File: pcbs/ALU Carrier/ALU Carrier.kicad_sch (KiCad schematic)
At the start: 2 parts, among them J1001 Conn_02x20_Odd_Even, J1002 Conn_02x20_Odd_Even

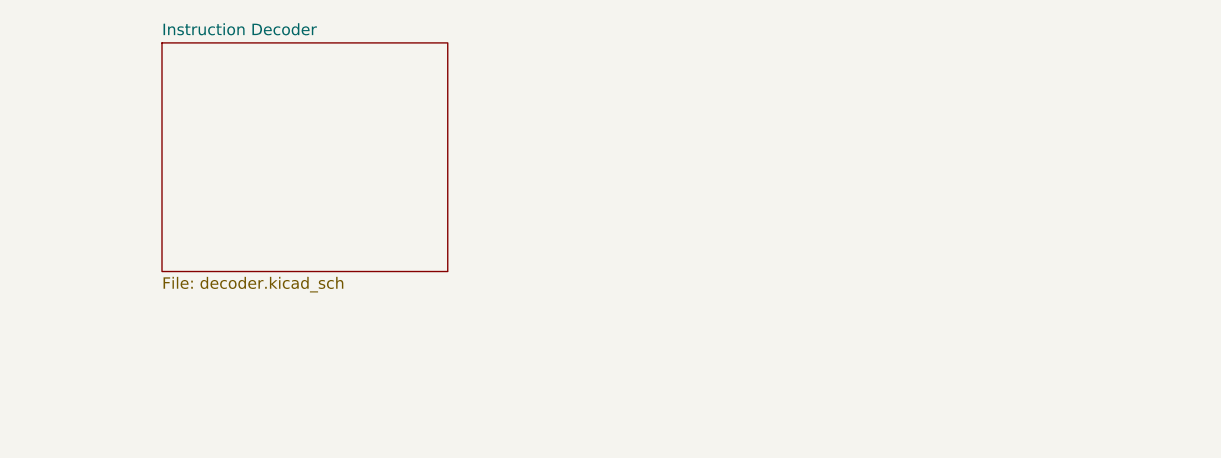
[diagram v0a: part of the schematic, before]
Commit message: Adding the adder
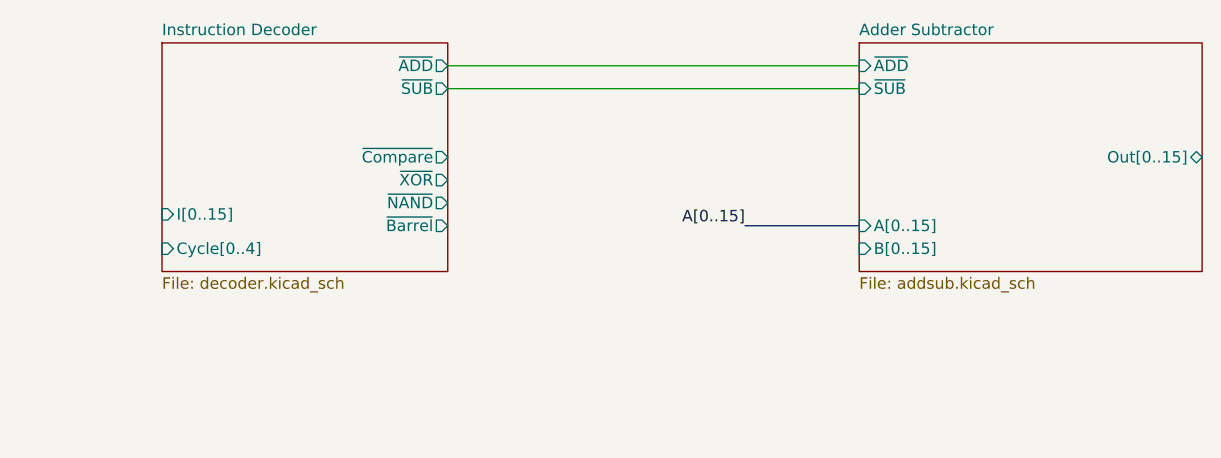
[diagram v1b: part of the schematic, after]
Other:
- added sheet Adder Subtractor (addsub.kicad_sch)
- sheet Instruction Decoder ports: added Cycle[0..4], I[0..15], ~{ADD}, ~{Barrel}, ~{Compare}, ~{NAND}, ~{SUB}, ~{XOR}; removed none
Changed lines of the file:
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@@
 	(generator "eeschema")
 	(generator_version "8.0")
-	(paper "A4")
+	(paper "A3")
 	(no_connect
 		(at 44.45 76.2)
@@
 	(wire
 		(pts
+			(xy 132.08 27.94) (xy 177.8 27.94)
+		)
+		(stroke
+			(width 0)
+			(type default)
+		)
+	)
+	(wire
+		(pts
 			(xy 44.45 128.27) (xy 46.99 128.27)
 		)
@@
 	(wire
 		(pts
+			(xy 132.08 30.48) (xy 177.8 30.48)
+		)
+		(stroke
+			(width 0)
+			(type default)
+		)
+	)
+	(wire
+		(pts
 			(xy 44.45 143.51) (xy 46.99 143.51)
 		)
@@
 		(pts
 			(xy 29.21 140.97) (xy 31.75 140.97)
+		)
+		(stroke
+			(width 0)
+			(type default)
+		)
+	)
+	(bus
+		(pts
+			(xy 165.1 45.72) (xy 177.8 45.72)
 		)
 		(stroke
@@
 	(label "I10"
 		(at 29.21 128.27 180)
+		(fields_autoplaced yes)
+		(effects
+			(font
+				(size 1.27 1.27)
+			)
+			(justify right bottom)
+		)
+	)
+	(label "A[0..15]"
+		(at 165.1 45.72 180)
 		(fields_autoplaced yes)
 		(effects
@@
 			)
 		)
+		(pin "I[0..15]" input
+			(at 100.33 44.45 180)
+			(effects
+				(font
+					(size 1.27 1.27)
+				)
+				(justify left)
+			)
+		)
+		(pin "Cycle[0..4]" input
+			(at 100.33 48.26 180)
+			(effects
+				(font
+					(size 1.27 1.27)
+				)
+				(justify left)
+			)
+		)
+		(pin "~{XOR}" output
+			(at 132.08 40.64 0)
+			(effects
+				(font
+					(size 1.27 1.27)
+				)
+				(justify right)
+			)
+		)
+		(pin "~{Compare}" output
+			(at 132.08 38.1 0)
+			(effects
+				(font
+					(size 1.27 1.27)
+				)
+				(justify right)
+			)
+		)
+		(pin "~{NAND}" output
+			(at 132.08 43.18 0)
+			(effects
+				(font
+					(size 1.27 1.27)
+				)
+				(justify right)
+			)
+		)
+		(pin "~{SUB}" output
+			(at 132.08 30.48 0)
+			(effects
+				(font
+					(size 1.27 1.27)
+				)
+				(justify right)
+			)
+		)
+		(pin "~{Barrel}" output
+			(at 132.08 45.72 0)
+			(effects
+				(font
+					(size 1.27 1.27)
+				)
+				(justify right)
+			)
+		)
+		(pin "~{ADD}" output
+			(at 132.08 27.94 0)
+			(effects
+				(font
+					(size 1.27 1.27)
+				)
+				(justify right)
+			)
+		)
 		(instances
 			(project "ALU Carrier"
@@
 				)
 			)
+		)
+	)
+	(sheet
+		(at 177.8 25.4)
+		(size 38.1 25.4)
+		(fields_autoplaced yes)
+		(stroke
+			(width 0.1524)
+			(type solid)
+		)
+		(fill
+			(color 0 0 0 0.0000)
+		)
+		(property "Sheetname" "Adder Subtractor"
+			(at 177.8 24.6884 0)
+			(effects
+				(font
+					(size 1.27 1.27)
+				)
+				(justify left bottom)
+			)
+		)
+		(property "Sheetfile" "addsub.kicad_sch"
+			(at 177.8 51.3846 0)
+			(effects
+				(font
+					(size 1.27 1.27)
+				)
+				(justify left top)
+			)
+		)
+		(pin "~{ADD}" input
+			(at 177.8 27.94 180)
+			(effects
+				(font
+					(size 1.27 1.27)
+				)
+				(justify left)
+			)
+		)
+		(pin "A[0..15]" input
+			(at 177.8 45.72 180)
+			(effects
+				(font
+					(size 1.27 1.27)
+				)
+				(justify left)
+			)
+		)
+		(pin "B[0..15]" input
+			(at 177.8 48.26 180)
+			(effects
+				(font
+					(size 1.27 1.27)
+				)
+				(justify left)
+			)
+		)
+		(pin "~{SUB}" input
+			(at 177.8 30.48 180)
+			(effects
+				(font
+					(size 1.27 1.27)
+				)
+				(justify left)
+			)
+		)
+		(pin "Out[0..15]" tri_state
+			(at 215.9 38.1 0)
+			(effects
+				(font
+					(size 1.27 1.27)
+				)
+				(justify right)
+			)
+		)
+		(instances
+			(project "ALU Carrier"
+				(path "/2be9e5f9-941e-4c29-a733-4c8d2e8b8610"
+					(page "3")
+				)
+			)

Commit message: Working...
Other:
- added sheet Comparator (compare.kicad_sch)
- added sheet XOR NAND (xornand.kicad_sch)
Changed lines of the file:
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@@
 	(generator_version "8.0")
 	(paper "A3")
+	(junction
+		(at 166.37 45.72)
+		(diameter 0)
+		(color 0 0 0 0)
+	)
 	(no_connect
 		(at 44.45 76.2)
@@
 		)
 	)
+	(bus
+		(pts
+			(xy 227.33 38.1) (xy 215.9 38.1)
+		)
+		(stroke
+			(width 0)
+			(type default)
+		)
+	)
 	(wire
 		(pts
@@
 	(wire
 		(pts
+			(xy 152.4 62.23) (xy 177.8 62.23)
+		)
+		(stroke
+			(width 0)
+			(type default)
+		)
+	)
+	(bus
+		(pts
+			(xy 166.37 76.2) (xy 166.37 45.72)
+		)
+		(stroke
+			(width 0)
+			(type default)
+		)
+	)
+	(wire
+		(pts
 			(xy 44.45 97.79) (xy 46.99 97.79)
 		)
@@
 	(wire
 		(pts
+			(xy 132.08 38.1) (xy 152.4 38.1)
+		)
+		(stroke
+			(width 0)
+			(type default)
+		)
+	)
+	(wire
+		(pts
 			(xy 44.45 107.95) (xy 46.99 107.95)
 		)
@@
 		)
 	)
+	(bus
+		(pts
+			(xy 215.9 72.39) (xy 227.33 72.39)
+		)
+		(stroke
+			(width 0)
+			(type default)
+		)
+	)
 	(wire
 		(pts
@@
 	(bus
 		(pts
-			(xy 165.1 45.72) (xy 177.8 45.72)
+			(xy 165.1 45.72) (xy 166.37 45.72)
 		)
 		(stroke
@@
 		)
 	)
+	(bus
+		(pts
+			(xy 177.8 76.2) (xy 166.37 76.2)
+		)
+		(stroke
+			(width 0)
+			(type default)
+		)
+	)
 	(wire
 		(pts
@@
 		)
 	)
+	(bus
+		(pts
+			(xy 227.33 72.39) (xy 227.33 38.1)
+		)
+		(stroke
+			(width 0)
+			(type default)
+		)
+	)
 	(wire
 		(pts
@@
 		)
 	)
+	(bus
+		(pts
+			(xy 166.37 45.72) (xy 177.8 45.72)
+		)
+		(stroke
+			(width 0)
+			(type default)
+		)
+	)
 	(wire
 		(pts
@@
 		(pts
 			(xy 44.45 53.34) (xy 46.99 53.34)
+		)
+		(stroke
+			(width 0)
+			(type default)
+		)
+	)
+	(wire
+		(pts
+			(xy 152.4 38.1) (xy 152.4 62.23)
 		)
 		(stroke
@@
 	)
 	(sheet
+		(at 177.8 58.42)
+		(size 38.1 24.13)
+		(fields_autoplaced yes)
+		(stroke
+			(width 0.1524)
+			(type solid)
+		)
+		(fill
+			(color 0 0 0 0.0000)
+		)
+		(property "Sheetname" "Comparator"
+			(at 177.8 57.7084 0)
+			(effects
+				(font
+					(size 1.27 1.27)
+				)
+				(justify left bottom)
+			)
+		)
+		(property "Sheetfile" "compare.kicad_sch"
+			(at 177.8 83.1346 0)
+			(effects
+				(font
+					(size 1.27 1.27)
+				)
+				(justify left top)
+			)
+		)
+		(pin "A[0..15]" input
+			(at 177.8 76.2 180)
+			(effects
+				(font
+					(size 1.27 1.27)
+				)
+				(justify left)
+			)
+		)
+		(pin "B[0..15]" input
+			(at 177.8 78.74 180)
+			(effects
+				(font
+					(size 1.27 1.27)
+				)
+				(justify left)
+			)
+		)
+		(pin "~{Compare}" input
+			(at 177.8 62.23 180)
+			(effects
+				(font
+					(size 1.27 1.27)
+				)
+				(justify left)
+			)
+		)
+		(pin "Out[0..15]" tri_state
+			(at 215.9 72.39 0)
+			(effects
+				(font
+					(size 1.27 1.27)
+				)
+				(justify right)
+			)
+		)
+		(instances
+			(project "ALU Carrier"
+				(path "/2be9e5f9-941e-4c29-a733-4c8d2e8b8610"
+					(page "4")
+				)
+			)
+		)
+	)
+	(sheet
 		(at 100.33 25.4)
 		(size 31.75 25.4)
@@
 				)
 			)
+		)
+	)
+	(sheet
+		(at 177.8 88.9)
+		(size 38.1 25.4)
+		(fields_autoplaced yes)
+		(stroke
+			(width 0.1524)
+			(type solid)
+		)
+		(fill
+			(color 0 0 0 0.0000)
+		)
+		(property "Sheetname" "XOR NAND"
+			(at 177.8 88.1884 0)
+			(effects
+				(font
+					(size 1.27 1.27)
+				)
+				(justify left bottom)
+			)
+		)
+		(property "Sheetfile" "xornand.kicad_sch"
+			(at 177.8 114.8846 0)
+			(effects
+				(font
+					(size 1.27 1.27)
+				)
+				(justify left top)
+			)
+		)
+		(instances
+			(project "ALU Carrier"
+				(path "/2be9e5f9-941e-4c29-a733-4c8d2e8b8610"
+					(page "5")
+				)
+			)

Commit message: Roughing out
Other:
- added sheet Barrel Shifter (barrel.kicad_sch)
- sheet XOR NAND ports: added A[0..15], B[0..15], Out[0..15], ~{NAND}, ~{XOR}; removed none

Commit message: Refactor
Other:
- added sheet Enabler (enabler.kicad_sch)
- sheet Instruction Decoder ports: added ~{Enable}; removed Cycle[0..4]

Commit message: Roughing out some layout
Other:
- added sheet Output Stage (output.kicad_sch)
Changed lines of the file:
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@@
+	)
+	(junction
+		(at 115.57 48.26)
+		(diameter 0)
+		(color 0 0 0 0)
 	)
 	(junction
@@
 		(color 0 0 0 0)
 	)
+	(junction
+		(at 191.77 68.58)
+		(diameter 0)
+		(color 0 0 0 0)
+	)
+	(junction
+		(at 248.92 76.2)
+		(diameter 0)
+		(color 0 0 0 0)
+	)
 	(no_connect
 		(at 44.45 76.2)
@@
 		)
 	)
+	(wire
+		(pts
+			(xy 115.57 27.94) (xy 261.62 27.94)
+		)
+		(stroke
+			(width 0)
+			(type default)
+		)
+	)
 	(bus
 		(pts
@@
 	(wire
 		(pts
+			(xy 261.62 64.77) (xy 273.05 64.77)
+		)
+		(stroke
+			(width 0)
+			(type default)
+		)
+	)
+	(wire
+		(pts
 			(xy 44.45 43.18) (xy 46.99 43.18)
 		)
@@
 	(wire
 		(pts
+			(xy 261.62 27.94) (xy 261.62 64.77)
+		)
+		(stroke
+			(width 0)
+			(type default)
+		)
+	)
+	(wire
+		(pts
 			(xy 44.45 68.58) (xy 46.99 68.58)
 		)
@@
 	(wire
 		(pts
+			(xy 115.57 48.26) (xy 121.92 48.26)
+		)
+		(stroke
+			(width 0)
+			(type default)
+		)
+	)
+	(wire
+		(pts
 			(xy 153.67 60.96) (xy 171.45 60.96)
 		)
@@
 	(wire
 		(pts
+			(xy 115.57 48.26) (xy 115.57 27.94)
+		)
+		(stroke
+			(width 0)
+			(type default)
+		)
+	)
+	(wire
+		(pts
 			(xy 44.45 71.12) (xy 46.99 71.12)
 		)
@@
 	(bus
 		(pts
+			(xy 248.92 76.2) (xy 248.92 58.42)
+		)
+		(stroke
+			(width 0)
+			(type default)
+		)
+	)
+	(bus
+		(pts
 			(xy 186.69 66.04) (xy 187.96 66.04)
 		)
@@
 		)
 	)
+	(bus
+		(pts
+			(xy 322.58 76.2) (xy 342.9 76.2)
+		)
+		(stroke
+			(width 0)
+			(type default)
+		)
+	)
 	(wire
 		(pts
@@
 	(bus
 		(pts
-			(xy 248.92 92.71) (xy 248.92 58.42)
+			(xy 248.92 92.71) (xy 248.92 76.2)
 		)
 		(stroke
@@
 		)
 	)
+	(bus
+		(pts
+			(xy 186.69 68.58) (xy 191.77 68.58)
+		)
+		(stroke
+			(width 0)
+			(type default)
+		)
+	)
 	(wire
 		(pts
@@
 	(wire
 		(pts
-			(xy 110.49 48.26) (xy 121.92 48.26)
+			(xy 110.49 48.26) (xy 115.57 48.26)
 		)
 		(stroke
@@
 		(pts
 			(xy 29.21 38.1) (xy 31.75 38.1)
+		)
+		(stroke
+			(width 0)
+			(type default)
+		)
+	)
+	(bus
+		(pts
+			(xy 248.92 76.2) (xy 273.05 76.2)
 		)
 		(stroke
@@
 		)
 	)
+	(label "C[0..15]"
+		(at 342.9 76.2 0)
+		(fields_autoplaced yes)
+		(effects
+			(font
+				(size 1.27 1.27)
+			)
+			(justify left bottom)
+		)
+	)
 	(label "A0"
 		(at 29.21 33.02 180)
@@
 			)
 			(justify left bottom)
+		)
+	)
+	(label "B[0..15]"
+		(at 186.69 68.58 180)
+		(fields_autoplaced yes)
+		(effects
+			(font
+				(size 1.27 1.27)
+			)
+			(justify right bottom)
 		)
 	)
@@
 				)
 			)
+		)
+	)
+	(sheet
+		(at 273.05 60.96)
+		(size 49.53 35.56)
+		(fields_autoplaced yes)
+		(stroke
+			(width 0.1524)
+			(type solid)
+		)
+		(fill
+			(color 0 0 0 0.0000)
+		)
+		(property "Sheetname" "Output Stage"
+			(at 273.05 60.2484 0)
+			(effects
+				(font
+					(size 1.27 1.27)
+				)
+				(justify left bottom)
+			)
+		)
+		(property "Sheetfile" "output.kicad_sch"
+			(at 273.05 97.1046 0)
+			(effects
+				(font
+					(size 1.27 1.27)
+				)
+				(justify left top)
+			)
+		)
+		(pin "~{Enable}" input
+			(at 273.05 64.77 180)
+			(effects
+				(font
+					(size 1.27 1.27)
+				)
+				(justify left)
+			)
+		)
+		(pin "Out[0..15]" input
+			(at 273.05 76.2 180)
+			(effects
+				(font
+					(size 1.27 1.27)
+				)
+				(justify left)
+			)
+		)
+		(pin "C[0..15]" tri_state
+			(at 322.58 76.2 0)
+			(effects
+				(font
+					(size 1.27 1.27)
+				)
+				(justify right)
+			)
+		)
+		(instances
+			(project "ALU Carrier"
+				(path "/2be9e5f9-941e-4c29-a733-4c8d2e8b8610"
+					(page "8")
+				)
+			)

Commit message: Thinking some more
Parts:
- added H1001, H1002, H1003, H1004: MountingHole, MountingHole:MountingHole_2.7mm_M2.5_ISO7380, symbol Mechanical:MountingHole
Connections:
- no-connect marks 5 -> 22
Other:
- sheet Enabler ports: added Cycle[2..3]; removed Cycle[0..4]
- sheet Instruction Decoder ports: added I[0..3]; removed I[0..15]

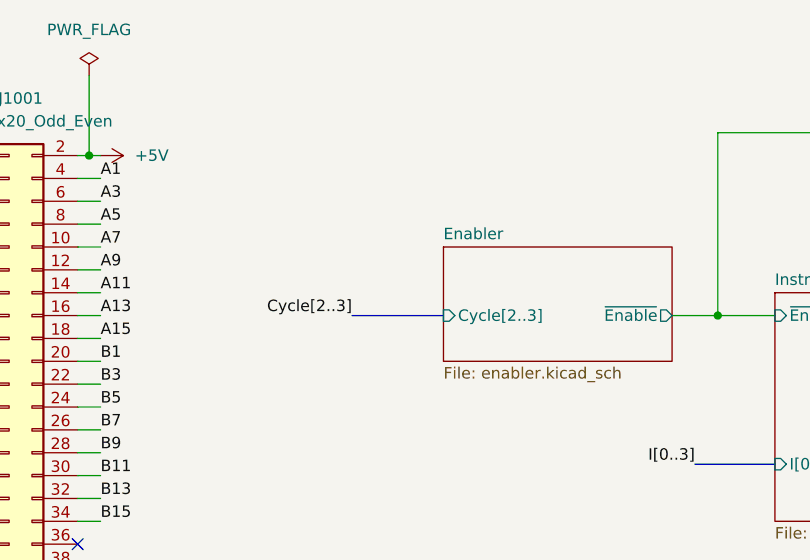
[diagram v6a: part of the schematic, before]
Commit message: Spotted nasty error in enable logic
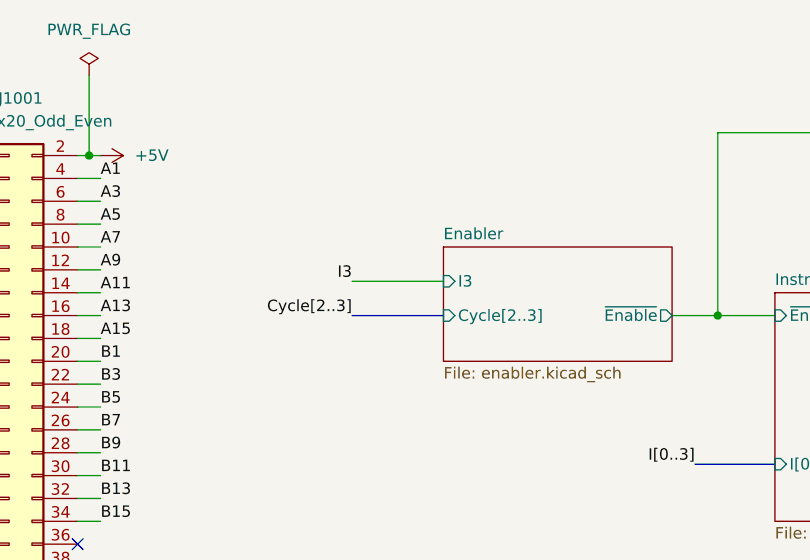
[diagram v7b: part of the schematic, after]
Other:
- sheet Enabler ports: added I3; removed none
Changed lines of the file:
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@@
+		)
+	)
+	(wire
+		(pts
+			(xy 74.93 44.45) (xy 85.09 44.45)
+		)
+		(stroke
+			(width 0)
+			(type default)
 		)
 	)
@@
 			)
 			(justify left bottom)
+		)
+	)
+	(label "I3"
+		(at 74.93 44.45 180)
+		(fields_autoplaced yes)
+		(effects
+			(font
+				(size 1.27 1.27)
+			)
+			(justify right bottom)
 		)
 	)
@@
 			(effects
 				(font
+					(size 1.27 1.27)
+				)
+				(justify left)
+			)
+		)
+		(pin "I3" input
+			(at 85.09 44.45 180)
+			(effects
+				(font
